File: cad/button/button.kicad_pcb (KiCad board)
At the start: 2 copper layers, 58 x 44 mm, 40 parts, among them J1 uSD_SPI, J2 SWD, Q1 DMC2038LVT, SW1 Button, U1 STM32L072KZTx, U2 PAM8302AAS

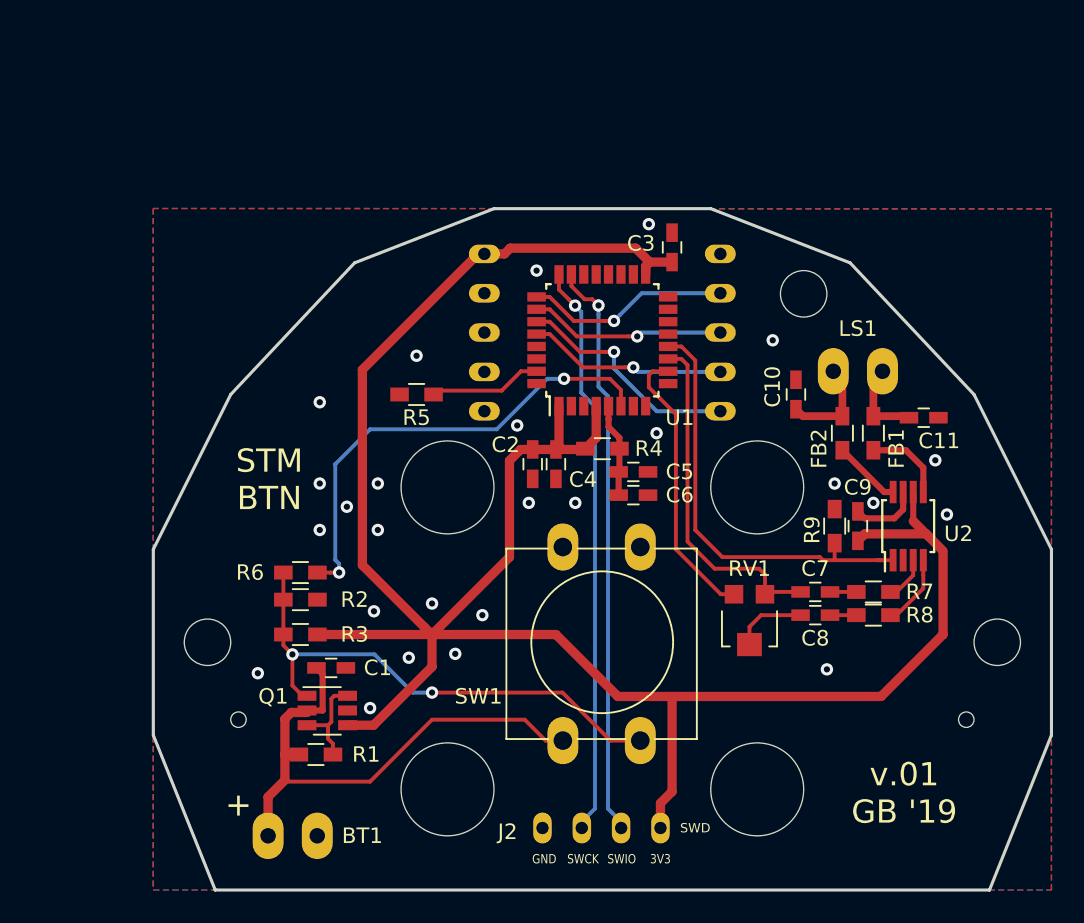
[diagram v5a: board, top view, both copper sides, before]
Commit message: prepare for other sdcard adapter
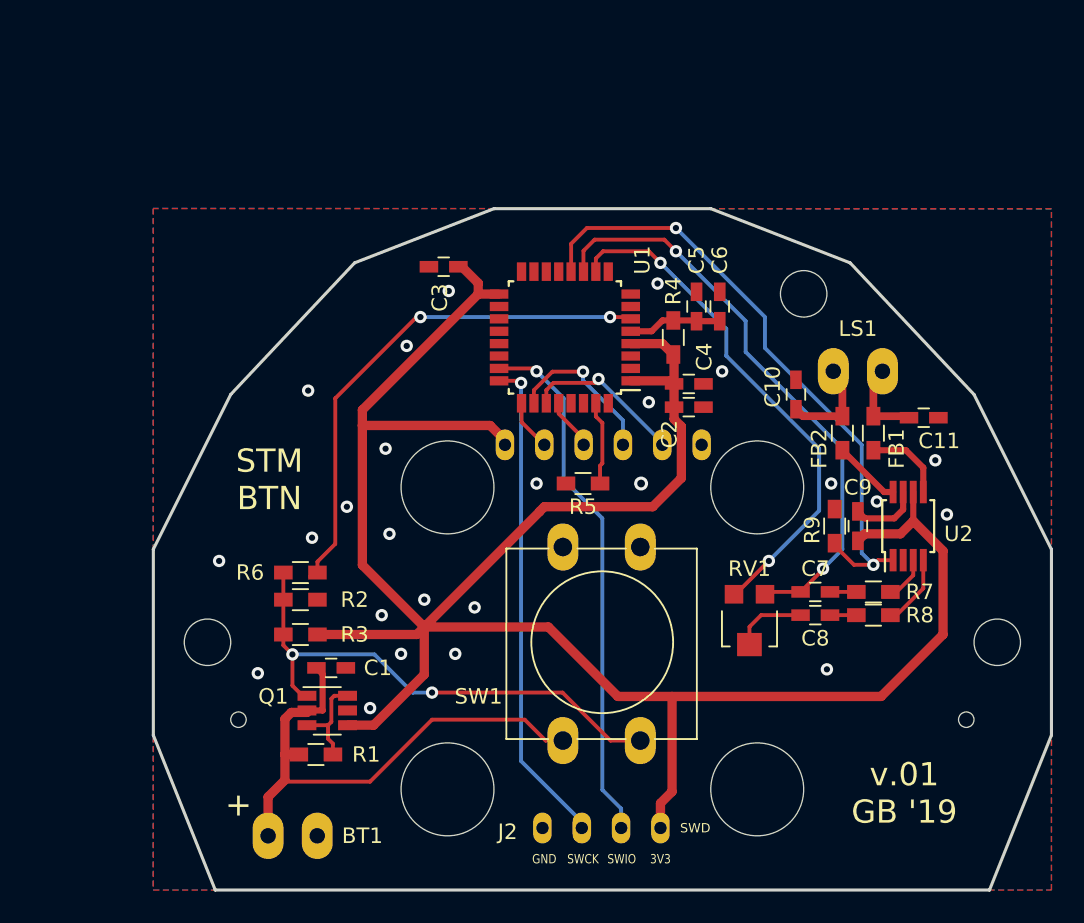
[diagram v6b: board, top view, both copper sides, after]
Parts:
- J1: value uSD_SPI -> Ali_uSD_SPI; footprint custom:PJRC_uSD_Adapter -> custom:Ali_uSD_Adapter
- moved C3 14.8 mm to (38.8, 26.8), turned to 0 degrees
- moved C6 13.4 mm to (56.6, 29.3), turned to 270 degrees
- moved R5 12.2 mm to (47.8, 40.8)
- moved C5 11.4 mm to (55.1, 29.3), turned to 270 degrees
- moved C2 10.7 mm to (54.6, 35.8), turned to 0 degrees
- moved C4 10.0 mm to (54.6, 34.3), turned to 180 degrees
- moved R4 8.52 mm to (53.6, 31.3), turned to 90 degrees
- moved U1 2.43 mm to (46.6, 31.3), turned to 180 degrees
- moved J1 1.64 mm to (49.1, 29.4)
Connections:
- J1 pad 2: SD_CS -> SD_MISO
- J1 pad 5: SD_MISO -> SD_CS
- J1 pad 6: (no net) -> +3V3
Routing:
- net SPK_IN+: track 22.3 -> 37.9 mm, vias 0 -> 2
- net SPK_IN-: track 18.3 -> 33.5 mm, vias 0 -> 2
- net SPK_SD: track 28.0 -> 40.6 mm, vias 0 -> 2
- net SD_CS: track 13.3 -> 3.29 mm, vias 1 -> 0
- net SD_MOSI: track 12.9 -> 3.35 mm, vias 1 -> 0
- net +3V3: track 144.2 -> 151.1 mm
- net /SWCLK: track 37.1 -> 31.8 mm
- net SD_MISO: track 14.9 -> 11.1 mm
- net /SWDIO: track 37.4 -> 34.3 mm
- net SD_SCK: track 12.7 -> 10.3 mm
- net Net-(R6-Pad2): track 31.2 -> 33.4 mm
- net /BOOT0: track 7.27 -> 5.42 mm
- net GND: vias 26 -> 25

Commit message: move to kicad 5 footprints
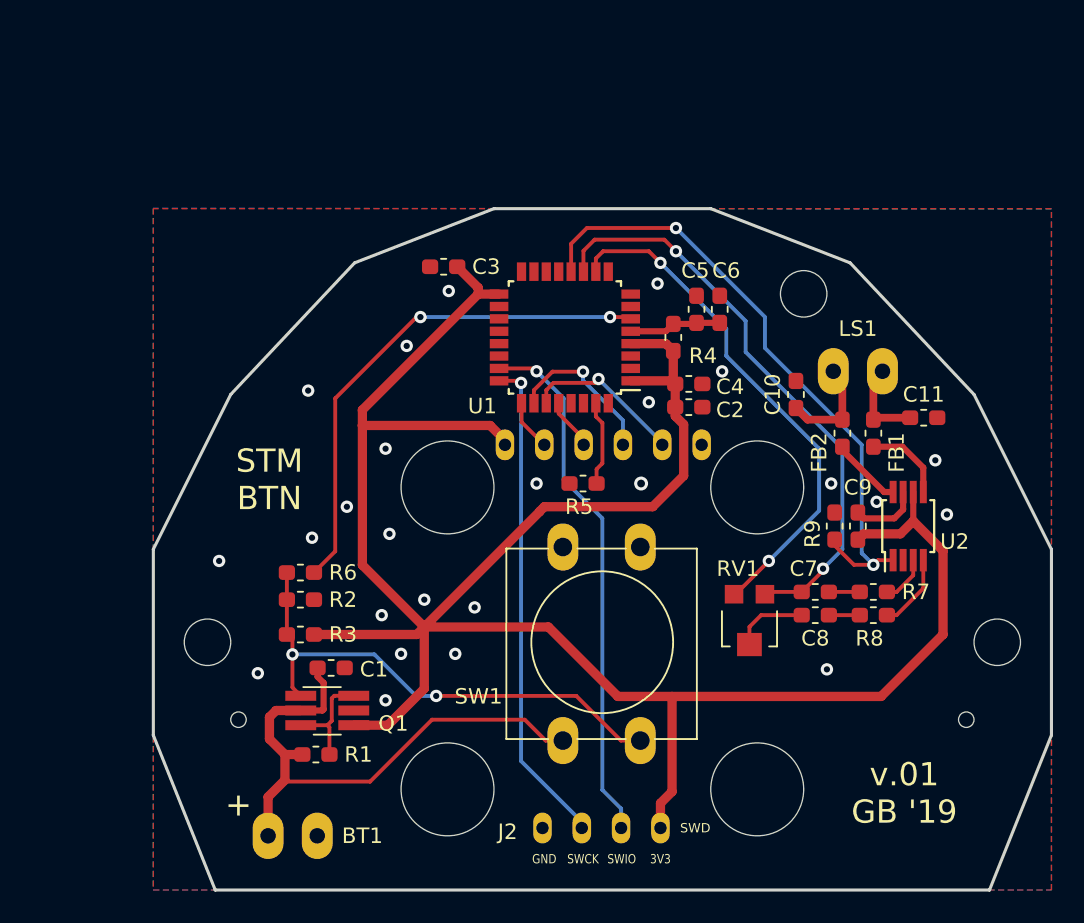
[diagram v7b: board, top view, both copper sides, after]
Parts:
- C1, C10, C11, C2, C3, C4, C5, C6, C7, C8, C9: footprint Capacitors_SMD:C_0603_HandSoldering -> Capacitor_SMD:C_0603_1608Metric_Pad1.05x0.95mm_HandSolder
- FB1, FB2: footprint Resistors_SMD:R_0603_HandSoldering -> Inductor_SMD:L_0603_1608Metric_Pad1.05x0.95mm_HandSolder
- Q1: footprint TO_SOT_Packages_SMD:TSOT-23-6 -> Package_TO_SOT_SMD:TSOT-23-6_HandSoldering
- R1, R2, R3, R4, R5, R6, R7, R8, R9: footprint Resistors_SMD:R_0603_HandSoldering -> Resistor_SMD:R_0603_1608Metric_Pad1.05x0.95mm_HandSolder
- U1: footprint Housings_QFP:LQFP-32_7x7mm_Pitch0.8mm -> Package_QFP:LQFP-32_7x7mm_P0.8mm
- U2: footprint Housings_SSOP:MSOP-8_3x3mm_Pitch0.65mm -> Package_SO:MSOP-8_3x3mm_P0.65mm
- moved C5 0.18 mm to (55.1, 29.5)
- moved C6 0.18 mm to (56.6, 29.5)
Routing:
- net /VBAT: track 34.6 -> 36.0 mm
- net SD_MISO: track 11.1 -> 10.5 mm
